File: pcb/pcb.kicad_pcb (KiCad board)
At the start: 2 copper layers, 63.8 x 43.2 mm, 39 parts, among them CN1 CP2102-BREAKOUT, CN2 TP4056, CN3 HX711_BREAKOUT, J1 BAT+, J10 GRN, J11 RED, J12 Load Cell, J2 BAT-, J3 Battery, J4 DS18B20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

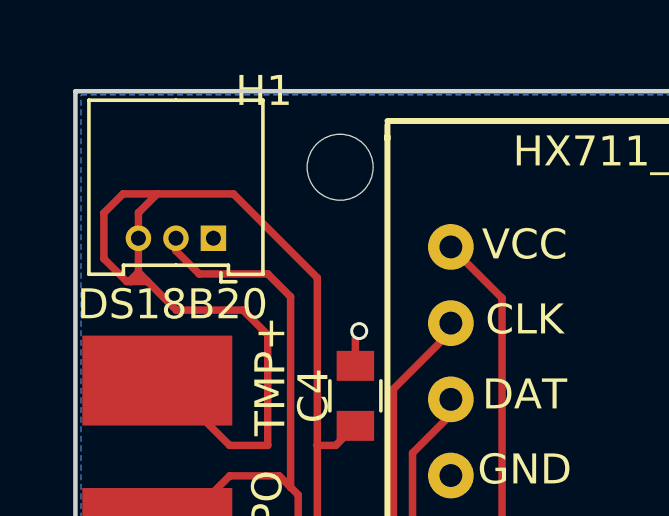
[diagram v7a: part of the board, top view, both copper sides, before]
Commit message: Move PCB text
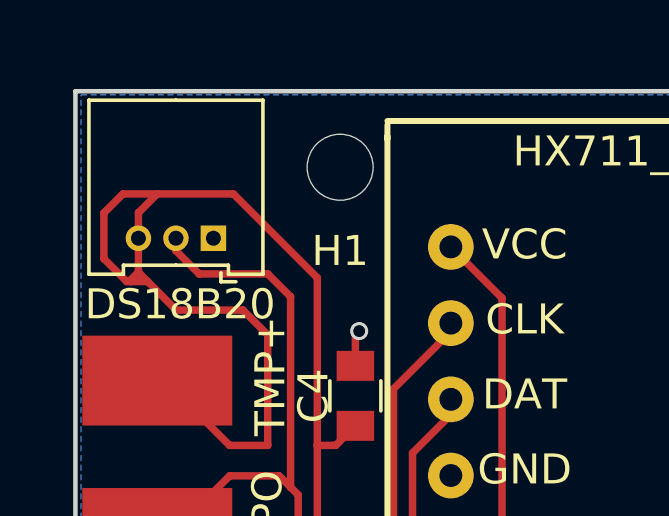
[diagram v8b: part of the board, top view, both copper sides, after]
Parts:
- moved ? 30.3 mm to (150.4, 80.4)
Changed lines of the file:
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@@
     (links 70)
     (no_connects 0)
-    (area 99.863999 58.638 182.188 114.438001)
+    (area 106.162999 65.462999 170.113001 108.813001)
     (thickness 1.6)
     (drawings 21)
@@
   (layers
     (0 F.Cu signal)
-    (31 B.Cu signal hide)
+    (31 B.Cu signal)
     (32 B.Adhes user)
     (33 F.Adhes user)
@@
     (aux_axis_origin 11.938 11.938)
     (grid_origin 11.938 11.938)
-    (visible_elements FFFFFFBF)
+    (visible_elements FFFFFFFF)
     (pcbplotparams
       (layerselection 0x010f0_80000001)
@@
       (effects (font (size 1 1) (thickness 0.15)))
     )
-    (fp_text value DS18B20 (at 1.364 -2.206 180) (layer F.SilkS)
+    (fp_text value DS18B20 (at 1.11 -2.206 180) (layer F.SilkS)
       (effects (font (size 1 1) (thickness 0.15)))
     )
@@
   )
   (module Symbols:OSHW-Logo2_7.3x6mm_SilkScreen (layer B.Cu)
-    (at 125.222 97.282 90)
+    (at 150.368 80.391 90)
     (descr "Open Source Hardware Symbol")
     (tags "Logo Symbol OSHW")
@@
     (descr "Mounting Hole 2.2mm, no annular, M2")
     (tags "mounting hole 2.2mm no annular m2")
-    (fp_text reference H1 (at -2.54 -2.54) (layer F.SilkS)
+    (fp_text reference H1 (at 0 2.794) (layer F.SilkS)
       (effects (font (size 1 1) (thickness 0.15)))
     )
@@
     (arrow2b (pts (xy 100.138 111.738) (xy 101.264504 111.151579)))
   )
-  (gr_text 1.0.0 (at 129.286 97.282 270) (layer B.SilkS)
+  (gr_text 1.0.0 (at 154.432 80.391 270) (layer B.SilkS)
     (effects (font (size 1 1) (thickness 0.15)) (justify mirror))
   )
-  (gr_text PendulumPCB (at 131.826 97.282 270) (layer B.SilkS)
+  (gr_text PendulumPCB (at 157.226 80.137 270) (layer B.SilkS)
     (effects (font (size 1.5 1.5) (thickness 0.3)) (justify mirror))
   )
